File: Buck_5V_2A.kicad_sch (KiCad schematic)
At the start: 9 parts, among them U3 TPS54202DDCR

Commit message: Route the board and apply the prototype PCB checklist fixes
Routing
- Route power (pours, In2 power areas, vias) and all signals; add a
  Signal net class (0.15 mm width/clearance) for low-speed nets.
- J8 expansion header is now a 2x8 near the MCU.

Checklist red flags
- Crystal Y3 moved beside U1's OSC pins with C5/C6 outboard and no
  other signals under it.
- Vias untented by default (tented only under silkscreen); 15 mil
  test vias on key signals, recorded as DRC exclusions.
- ESD: U6/U7 split into four USBLC6-2SC6 (U6, U11, U7, U12), one per
  connector, with VBUS caps C50/C51; R12/R13 moved next to J13.
- GND test loop TP3 moved to the top edge beside J5.

Improvements
- Encoder connectors J7/J15 changed to keyed JST XH S4B side-entry.
- 43 passives/LEDs/FB2 moved from 0603 to 0805 (MPNs updated).
- Fifth M3 mounting hole H5 under J8.
- +3.3VA rerouted away from the crystal; acute track angles removed.
- Datasheet links filled in; silkscreen pin labels, pin maps, team
  names and date; reference labels cleared off pads and vias.
- Custom DRC rule for the J7/J15 silkscreen edge overhang.
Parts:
- C15: footprint Capacitor_SMD:C_0603_1608Metric -> Capacitor_SMD:C_0805_2012Metric; MPN C1608X7R1H104K080AA -> C0805C104K5RACTU; Manufacturer TDK -> KEMET
- C16: footprint Capacitor_SMD:C_0603_1608Metric -> Capacitor_SMD:C_0805_2012Metric; MPN GRM1885C1H680JA01D -> C0805C680J5GACTU; Manufacturer Murata -> KEMET
- C49: footprint Capacitor_SMD:C_0603_1608Metric -> Capacitor_SMD:C_0805_2012Metric; MPN C0603C104K5RACTU -> C0805C104K5RACTU
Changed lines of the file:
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@@
 			)
 		)
-		(property "Footprint" "Capacitor_SMD:C_0603_1608Metric"
+		(property "Footprint" "Capacitor_SMD:C_0805_2012Metric"
 			(at 111.76 88.9 0)
 			(hide yes)
@@
 			)
 		)
-		(property "Datasheet" "~"
+		(property "Datasheet" "https://content.kemet.com/datasheets/KEM_C1002_X7R_SMD.pdf"
 			(at 111.76 88.9 0)
 			(hide yes)
@@
 			)
 		)
-		(property "MPN" "C0603C104K5RACTU"
+		(property "MPN" "C0805C104K5RACTU"
 			(at 111.76 88.9 0)
 			(hide yes)
@@
 			)
 		)
-		(property "Footprint" "Capacitor_SMD:C_0603_1608Metric"
+		(property "Footprint" "Capacitor_SMD:C_0805_2012Metric"
 			(at 182.58 88.9 0)
 			(hide yes)
@@
 			)
 		)
-		(property "Datasheet" "https://search.murata.co.jp/Ceramy/image/img/A01X/G101/ENG/GRM1885C1H680JA01-01A.pdf"
+		(property "Datasheet" "https://content.kemet.com/datasheets/KEM_C1003_C0G_SMD.pdf"
 			(at 181.61 85.09 0)
 			(hide yes)
@@
 			)
 		)
-		(property "Manufacturer" "Murata"
+		(property "Manufacturer" "KEMET"
 			(at 181.61 85.09 0)
 			(hide yes)
@@
 			)
 		)
-		(property "MPN" "GRM1885C1H680JA01D"
+		(property "MPN" "C0805C680J5GACTU"
 			(at 181.61 85.09 0)
 			(hide yes)
@@
 			)
 		)
-		(property "Footprint" "Capacitor_SMD:C_0603_1608Metric"
+		(property "Footprint" "Capacitor_SMD:C_0805_2012Metric"
 			(at 167.64 80.31 0)
 			(hide yes)
@@
 			)
 		)
-		(property "Datasheet" "https://product.tdk.com/en/search/capacitor/ceramic/mlcc/info?part_no=C1608X7R1H104K080AA"
+		(property "Datasheet" "https://content.kemet.com/datasheets/KEM_C1002_X7R_SMD.pdf"
 			(at 163.83 81.28 0)
 			(hide yes)
@@
 			)
 		)
-		(property "Manufacturer" "TDK"
+		(property "Manufacturer" "KEMET"
 			(at 163.83 81.28 0)
 			(hide yes)
@@
 			)
 		)
-		(property "MPN" "C1608X7R1H104K080AA"
+		(property "MPN" "C0805C104K5RACTU"
 			(at 163.83 81.28 0)
 			(hide yes)

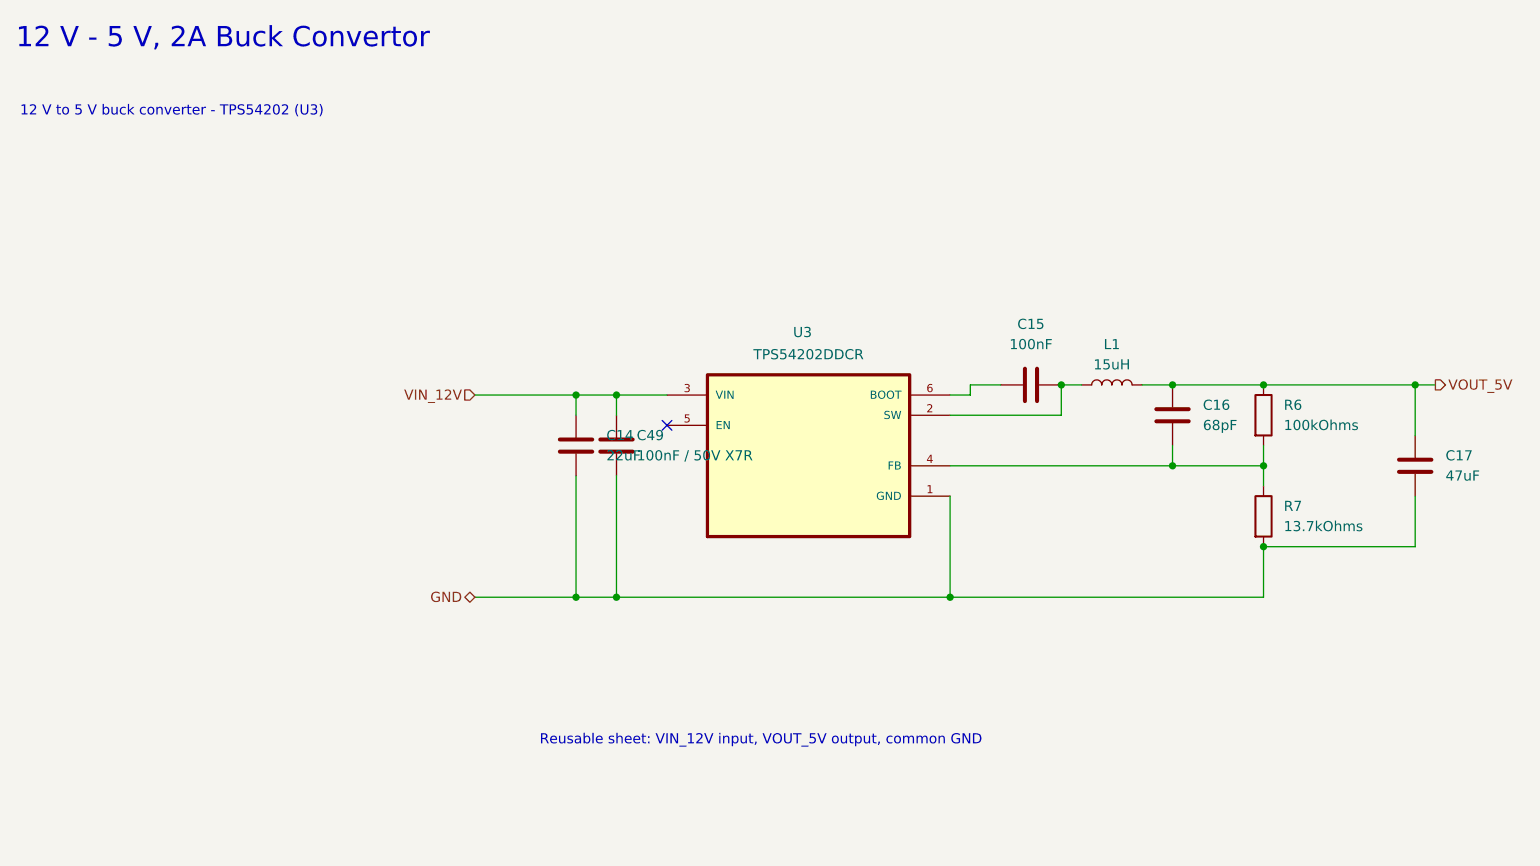
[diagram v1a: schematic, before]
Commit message: Replace out-of-stock buck converters with in-stock TI parts
TPSM63606 (U2, U5) and TPS54202 (U3) are out of stock at DigiKey.

- U2 (Pi 5 V) and U5 (AUX 5 V), 6 A: TPS56637RPAR with Wurth
  74439387033 3.3 uH, 2x 10 uF + 100 nF in, 47 uF out, 73.2k/10k
  feedback with 20k + 100 pF feed-forward, 100k PG pull-up. Values
  from TI WEBENCH (10-15 V in, 5 V 6 A); load-step sim 0.6->6 A
  stays within 4.91-5.06 V.
- U3 (+5V_SYS), 2 A: TPS54202HDDCR with TDK VLS6045EX-100M 10 uH,
  22 uF in, 47 uF out, 100k/13.7k + 68 pF, and a new 442k EN pull-up
  (R63) since the H version's EN is pulled down internally. Load-step
  sim 0.2->2 A stays within 4.72-5.21 V.
- New TPS56637 symbol, RPA0010A footprint (TI land pattern) and
  WE-XHMI-7070 footprint (Wurth land pattern).
- Layout follows the datasheet layout examples: TPS56637 Figure 34
  (VIN/Cin, inductor/Cout, AGND island, via arrays, inner-layer
  mirrors) and TPS54202H Figure 10-1 (SW through vias on an inner
  pour to the inductor, caps between GND and VIN copper).
- U5 moved below J8; PB7, PI_BOOT0, USART2_RX and the +5V_SYS feed
  rerouted around the new parts. New PG/EN resistors are R61-R63 to
  avoid the refs used on feat/battery-monitor-interior-light.
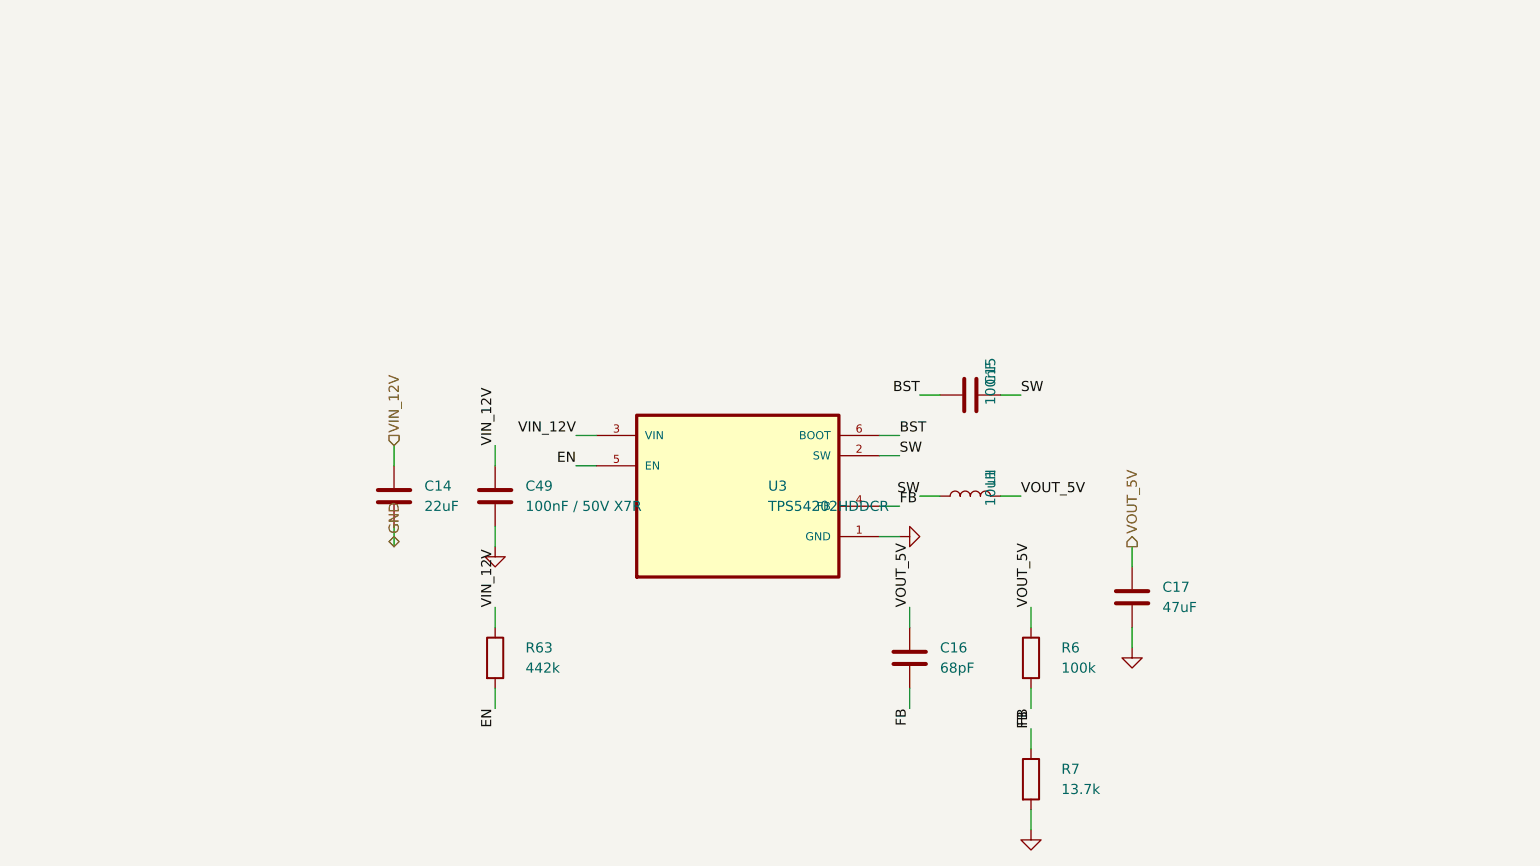
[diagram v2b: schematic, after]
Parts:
- added R63: 442k, Resistor_SMD:R_0805_2012Metric, symbol Device:R
- C14: footprint project_footprints:C_TDK_C5750X7R1H226M250KB -> Capacitor_SMD:C_1210_3225Metric; MPN C5750X7R1H226M250KB -> GRM32ER61E226KE15L; Manufacturer TDK -> Murata; Specification 22uF / 50V X7R -> 22uF / 25V X5R 1210 (Cin)
- C15: Specification 100nF / 50V X7R -> 100nF / 50V X7R (Cboot)
- C16: Specification 68pF / 50V C0G -> 68pF / 50V C0G (Cff)
- C17: footprint project_footprints:C_Murata_GRM32ER71A476ME15 -> Capacitor_SMD:C_1210_3225Metric; MPN GRM32ER71A476ME15L -> GRM32ER61C476KE15L; Specification 47uF / 10V X7R -> 47uF / 16V X5R 1210 (Cout)
- L1: value 15uH -> 10uH; footprint Inductor_SMD:L_Coilcraft_XAL6060-XXX -> Inductor_SMD:L_TDK_VLS6045EX_VLS6045AF; MPN XAL6060-153MEC -> VLS6045EX-100M; Manufacturer Coilcraft -> TDK; Specification 15uH / 20% -> 10uH 47mOhm 3.4A VLS6045EX 6x6
- R6: value 100kOhms -> 100k; MPN (none) -> RC0805FR-07100KL; Manufacturer (none) -> Yageo; Specification (none) -> 100k 1% (Rfbt)
- R7: value 13.7kOhms -> 13.7k; MPN (none) -> RC0805FR-0713K7L; Manufacturer (none) -> Yageo; Specification (none) -> 13.7k 1% (Rfbb)
- U3: value TPS54202DDCR -> TPS54202HDDCR; Availability In Stock -> (none); Check_prices https://www.snapeda.com/parts/TPS54202DDCR/Texas+Instrument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 -> (none); Description_1 4.5V to 28V Input, 2A Output, EMI Friendly Synchronous Step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 -> (none); Design Notes Feedback divider R6 100k / R7 13.7k sets about 4.95 V assum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 -> (none); Key Specs VIN 4.5-28 V; VOUT 0.6-26 V adjustable; IOUT max 2 A; fixed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 -> (none); MF Texas Instruments -> (none); MP TPS54202DDCR -> (none); MPN TPS54202DDCR -> TPS54202HDDCR; Package SOT-23-THN-6 Texas Instruments -> (none); Price None -> (none); Product Page https://www.ti.com/product/TPS54202 -> (none); SnapEDA_Link https://www.snapeda.com/parts/TPS54202DDCR/Texas+Instrument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 -> (none); Specification (none) -> 2 A buck, 500 kHz; Used In Sheet Buck_5V_2A: 12 V in, +5V_SYS net out (feeds LDO sheet) -> (none)
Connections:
- net VIN_12V: now also R63.1
- net VOUT_5V: now also L1.2; no longer L1.1
- net FB: now reaches C16.2, R6.2, R7.1, U3.4 (FB)
- net SW: now reaches C15.2, U3.2 (SW)
- net SW: now also L1.1; no longer L1.2
- net EN: now reaches U3.5 (EN)
- net EN: now also R63.2
- net BST: now reaches C15.1, U3.6 (BOOT)
- no-connect marks 1 -> 0
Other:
- note removed: "12 V - 5 V, 2A Buck Convertor"
- note removed: "12 V to 5 V buck converter - TPS54202 (U3)"
- note removed: "Reusable sheet: VIN_12V input, VOUT_5V output, common GND"
- moved on the sheet: C14, C15, C16, C17, C49, L1, R6, R7, U3
